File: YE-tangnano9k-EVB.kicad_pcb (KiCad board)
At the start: 2 copper layers, 95 x 72 mm, 23 parts, among them J1 Conn_01x24_Socket, J2 Conn_01x24_Socket, Q1 2SC1815, SW1 SW_SPDT, SW2 SW_Push, SW3 SW_Push, U1 Tang Nano 9K, U2 OSL40391-IRA

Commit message: 塗りつぶしをmeshに変更
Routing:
- net GND: track 5.08 -> 9179.2 mm
- removed copper zone on B.Cu, net GND

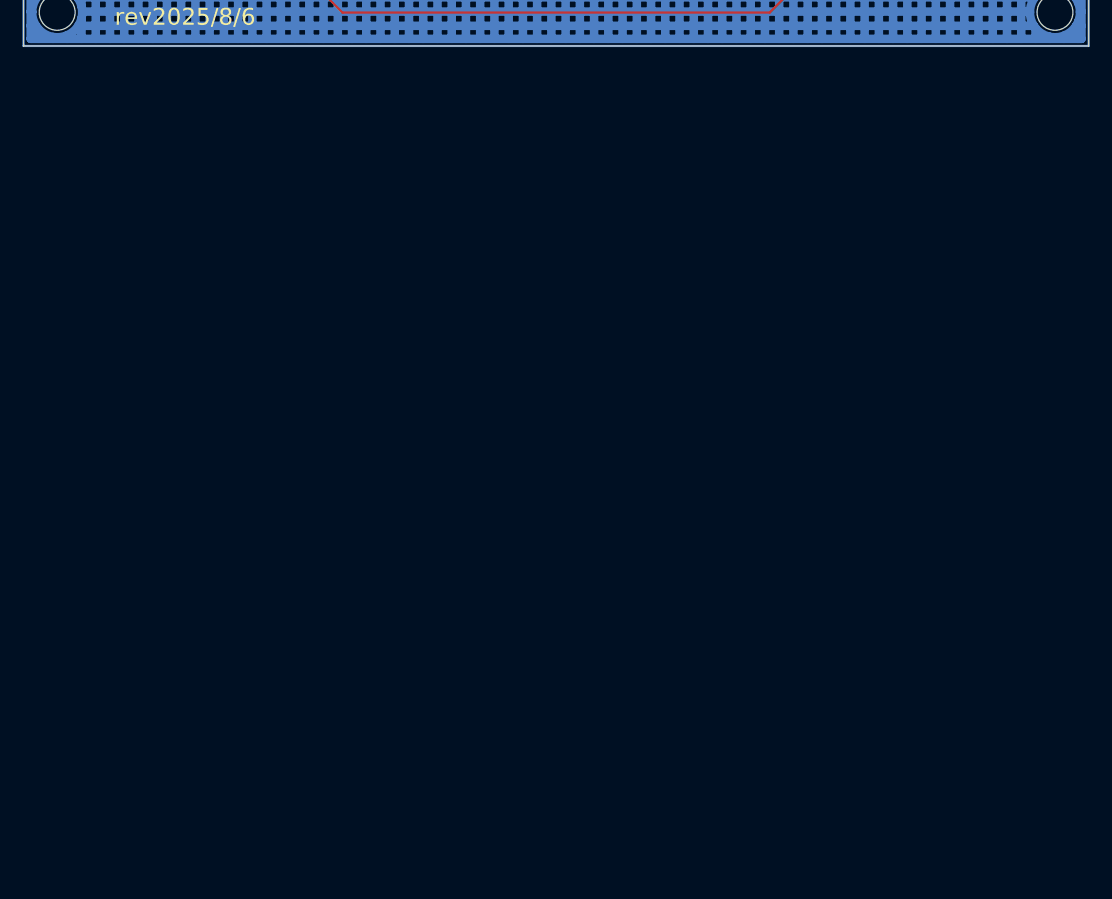
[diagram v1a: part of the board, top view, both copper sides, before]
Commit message: meshのみを下に置いとく
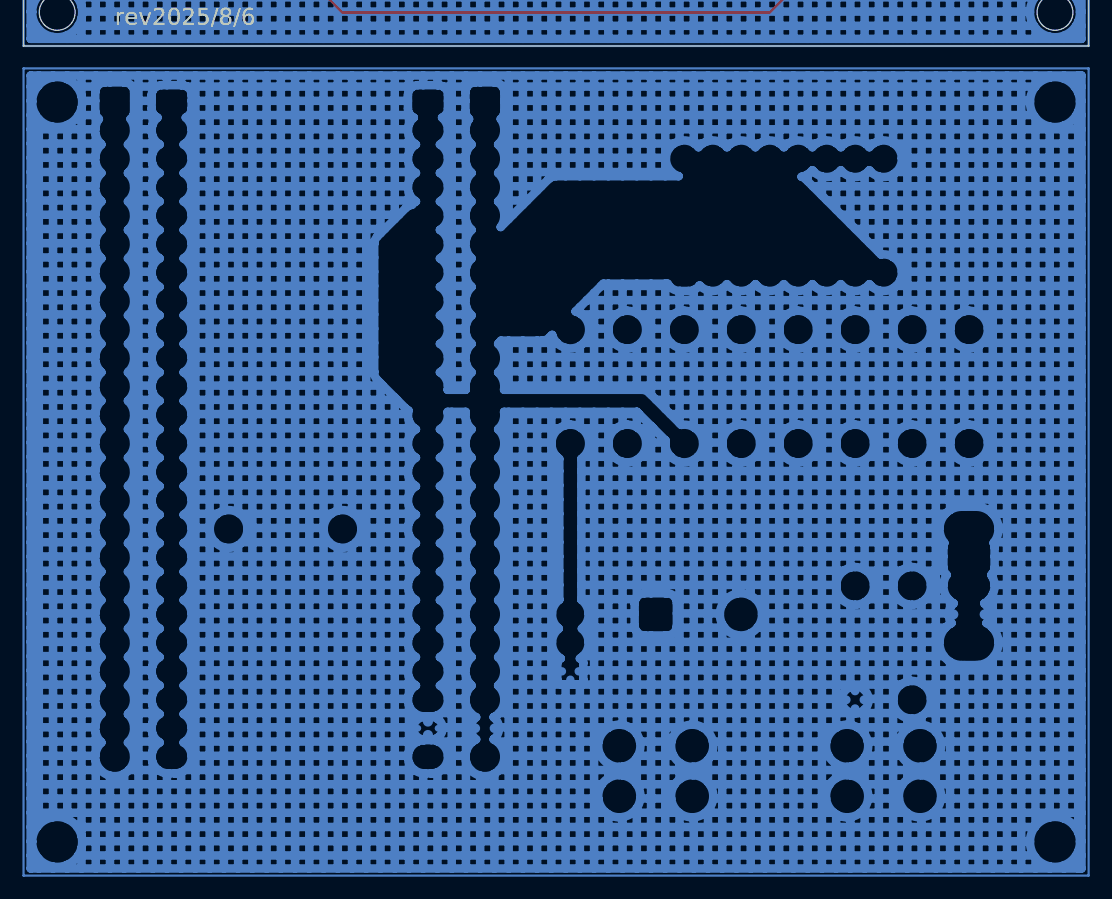
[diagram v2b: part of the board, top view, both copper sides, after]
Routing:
- net (no net): track 0.00 -> 9174.1 mm
